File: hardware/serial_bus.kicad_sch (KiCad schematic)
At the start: 15 parts, among them Q14 BC547, Q15 BC547, Q16 BC547, U2 74LS06N, U8 74LS06N

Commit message: Rev.E. Updated specifications document and hardware design.
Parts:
- Q14, Q15, Q16: value BC547 -> (none); footprint Package_TO_SOT_THT:TO-92_Inline_Wide -> (none)
- R52: footprint Resistor_THT:R_Axial_DIN0207_L6.3mm_D2.5mm_P10.16mm_Horizontal -> (none)
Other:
- note added: "1W"
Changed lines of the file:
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@@
+    (effects (font (size 1.27 1.27)) (justify left bottom))
+  )
+  (text "1W" (at 124.46 80.01 0)
     (effects (font (size 1.27 1.27)) (justify left bottom))
   )
@@
       (effects (font (size 1.27 1.27)) (justify left))
     )
-    (property "Value" "BC547" (id 1) (at 70.8914 67.183 0)
-      (effects (font (size 1.27 1.27)) (justify left))
-    )
-    (property "Footprint" "Package_TO_SOT_THT:TO-92_Inline_Wide" (id 2) (at 71.12 67.945 0)
+    (property "Value" "" (id 1) (at 70.8914 67.183 0)
+      (effects (font (size 1.27 1.27)) (justify left))
+    )
+    (property "Footprint" "" (id 2) (at 71.12 67.945 0)
       (effects (font (size 1.27 1.27) italic) (justify left) hide)
     )
@@
     (property "Reference" "R52" (id 0) (at 125.73 70.9422 90))
     (property "Value" "560R" (id 1) (at 125.73 73.2536 90))
-    (property "Footprint" "Resistor_THT:R_Axial_DIN0207_L6.3mm_D2.5mm_P10.16mm_Horizontal" (id 2) (at 125.73 77.978 90)
+    (property "Footprint" "" (id 2) (at 125.73 77.978 90)
       (effects (font (size 1.27 1.27)) hide)
     )
@@
       (effects (font (size 1.27 1.27)) (justify left))
     )
-    (property "Value" "BC547" (id 1) (at 70.8914 97.663 0)
-      (effects (font (size 1.27 1.27)) (justify left))
-    )
-    (property "Footprint" "Package_TO_SOT_THT:TO-92_Inline_Wide" (id 2) (at 71.12 98.425 0)
+    (property "Value" "" (id 1) (at 70.8914 97.663 0)
+      (effects (font (size 1.27 1.27)) (justify left))
+    )
+    (property "Footprint" "" (id 2) (at 71.12 98.425 0)
       (effects (font (size 1.27 1.27) italic) (justify left) hide)
     )
@@
     (in_bom yes) (on_board yes)
     (property "Reference" "Q14" (id 0) (at 50.8 44.069 90))
-    (property "Value" "BC547" (id 1) (at 50.8 46.3804 90))
-    (property "Footprint" "Package_TO_SOT_THT:TO-92_Inline_Wide" (id 2) (at 48.895 43.18 0)
+    (property "Value" "" (id 1) (at 50.8 46.3804 90))
+    (property "Footprint" "" (id 2) (at 48.895 43.18 0)
       (effects (font (size 1.27 1.27) italic) (justify left) hide)
     )

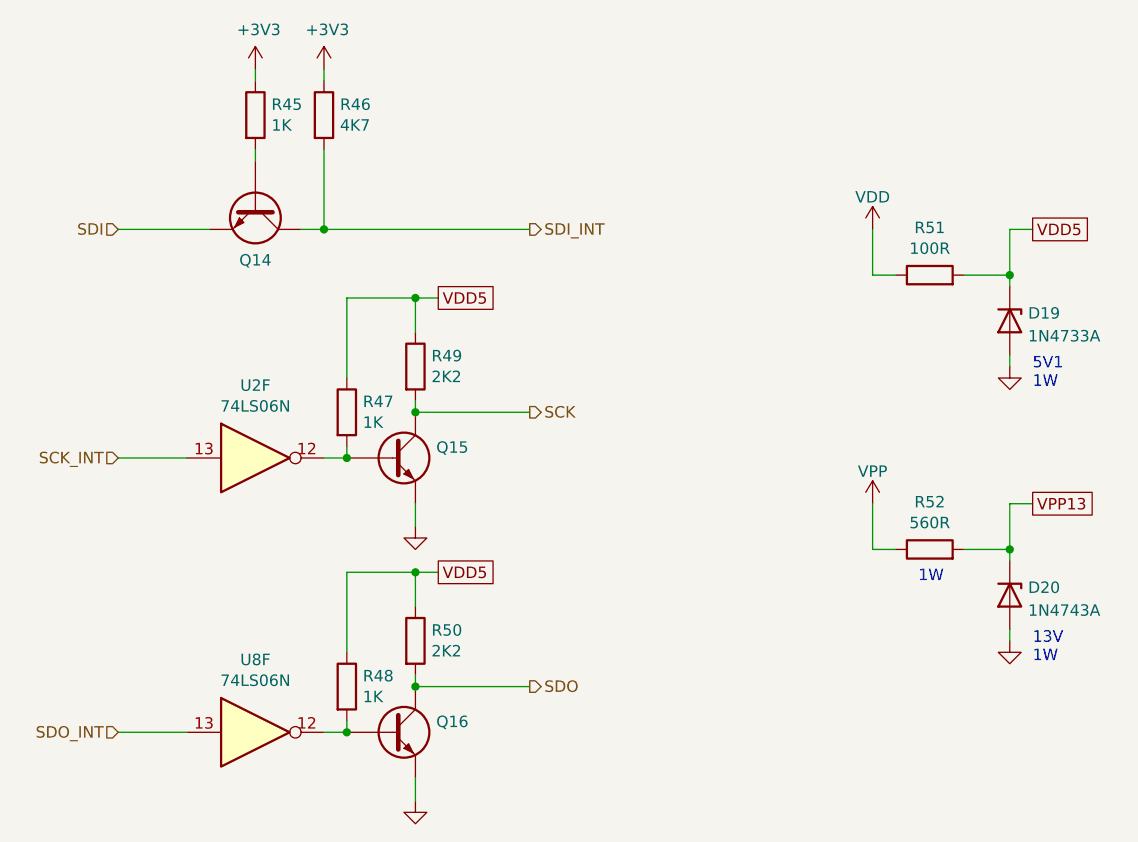
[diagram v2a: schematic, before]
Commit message: Rev.E. Updated R51 wattage.
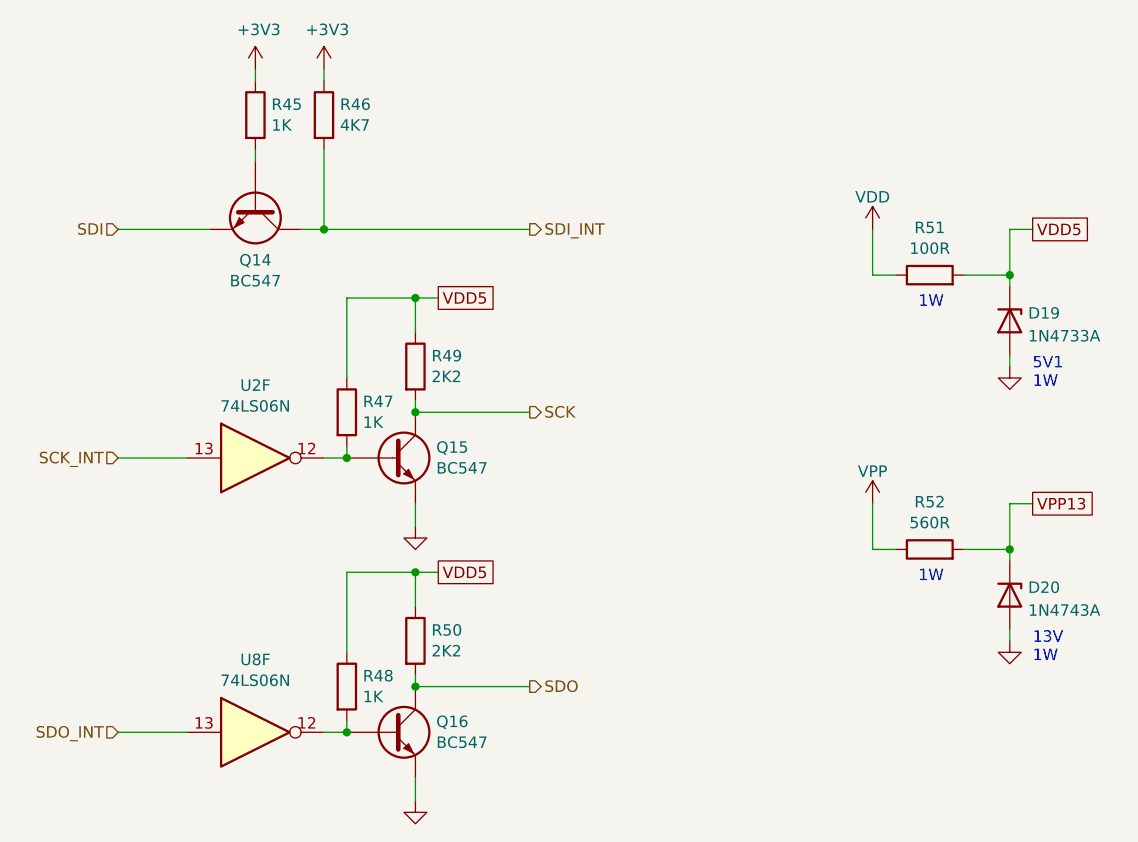
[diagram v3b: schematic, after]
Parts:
- Q14, Q15, Q16: value (none) -> BC547; footprint (none) -> Package_TO_SOT_THT:TO-92_Inline_Wide
- R52: footprint (none) -> Resistor_THT:R_Axial_DIN0309_L9.0mm_D3.2mm_P15.24mm_Horizontal
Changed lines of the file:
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@@
+    (effects (font (size 1.27 1.27)) (justify left bottom))
+  )
+  (text "1W" (at 124.46 49.53 0)
     (effects (font (size 1.27 1.27)) (justify left bottom))
   )
@@
       (effects (font (size 1.27 1.27)) (justify left))
     )
-    (property "Value" "" (id 1) (at 70.8914 67.183 0)
-      (effects (font (size 1.27 1.27)) (justify left))
-    )
-    (property "Footprint" "" (id 2) (at 71.12 67.945 0)
+    (property "Value" "BC547" (id 1) (at 70.8914 67.183 0)
+      (effects (font (size 1.27 1.27)) (justify left))
+    )
+    (property "Footprint" "Package_TO_SOT_THT:TO-92_Inline_Wide" (id 2) (at 71.12 67.945 0)
       (effects (font (size 1.27 1.27) italic) (justify left) hide)
     )
@@
     (property "Reference" "R52" (id 0) (at 125.73 70.9422 90))
     (property "Value" "560R" (id 1) (at 125.73 73.2536 90))
-    (property "Footprint" "" (id 2) (at 125.73 77.978 90)
+    (property "Footprint" "Resistor_THT:R_Axial_DIN0309_L9.0mm_D3.2mm_P15.24mm_Horizontal" (id 2) (at 125.73 77.978 90)
       (effects (font (size 1.27 1.27)) hide)
     )
@@
       (effects (font (size 1.27 1.27)) (justify left))
     )
-    (property "Value" "" (id 1) (at 70.8914 97.663 0)
-      (effects (font (size 1.27 1.27)) (justify left))
-    )
-    (property "Footprint" "" (id 2) (at 71.12 98.425 0)
+    (property "Value" "BC547" (id 1) (at 70.8914 97.663 0)
+      (effects (font (size 1.27 1.27)) (justify left))
+    )
+    (property "Footprint" "Package_TO_SOT_THT:TO-92_Inline_Wide" (id 2) (at 71.12 98.425 0)
       (effects (font (size 1.27 1.27) italic) (justify left) hide)
     )
@@
     (in_bom yes) (on_board yes)
     (property "Reference" "Q14" (id 0) (at 50.8 44.069 90))
-    (property "Value" "" (id 1) (at 50.8 46.3804 90))
-    (property "Footprint" "" (id 2) (at 48.895 43.18 0)
+    (property "Value" "BC547" (id 1) (at 50.8 46.3804 90))
+    (property "Footprint" "Package_TO_SOT_THT:TO-92_Inline_Wide" (id 2) (at 48.895 43.18 0)
       (effects (font (size 1.27 1.27) italic) (justify left) hide)
     )
